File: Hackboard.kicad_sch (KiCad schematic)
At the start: 70 parts, among them J1 Conn_01x23_Socket, J2 Micro_SD_Card, J3 Conn_01x32_Socket, J4 Conn_01x08_Socket, J5 Conn_01x02_Pin, J6 USB_C_Receptacle_USB2.0_16P, J7 Barrel_Jack_Switch, Q1 NMOS, Q2 NMOS, Q3 NMOS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

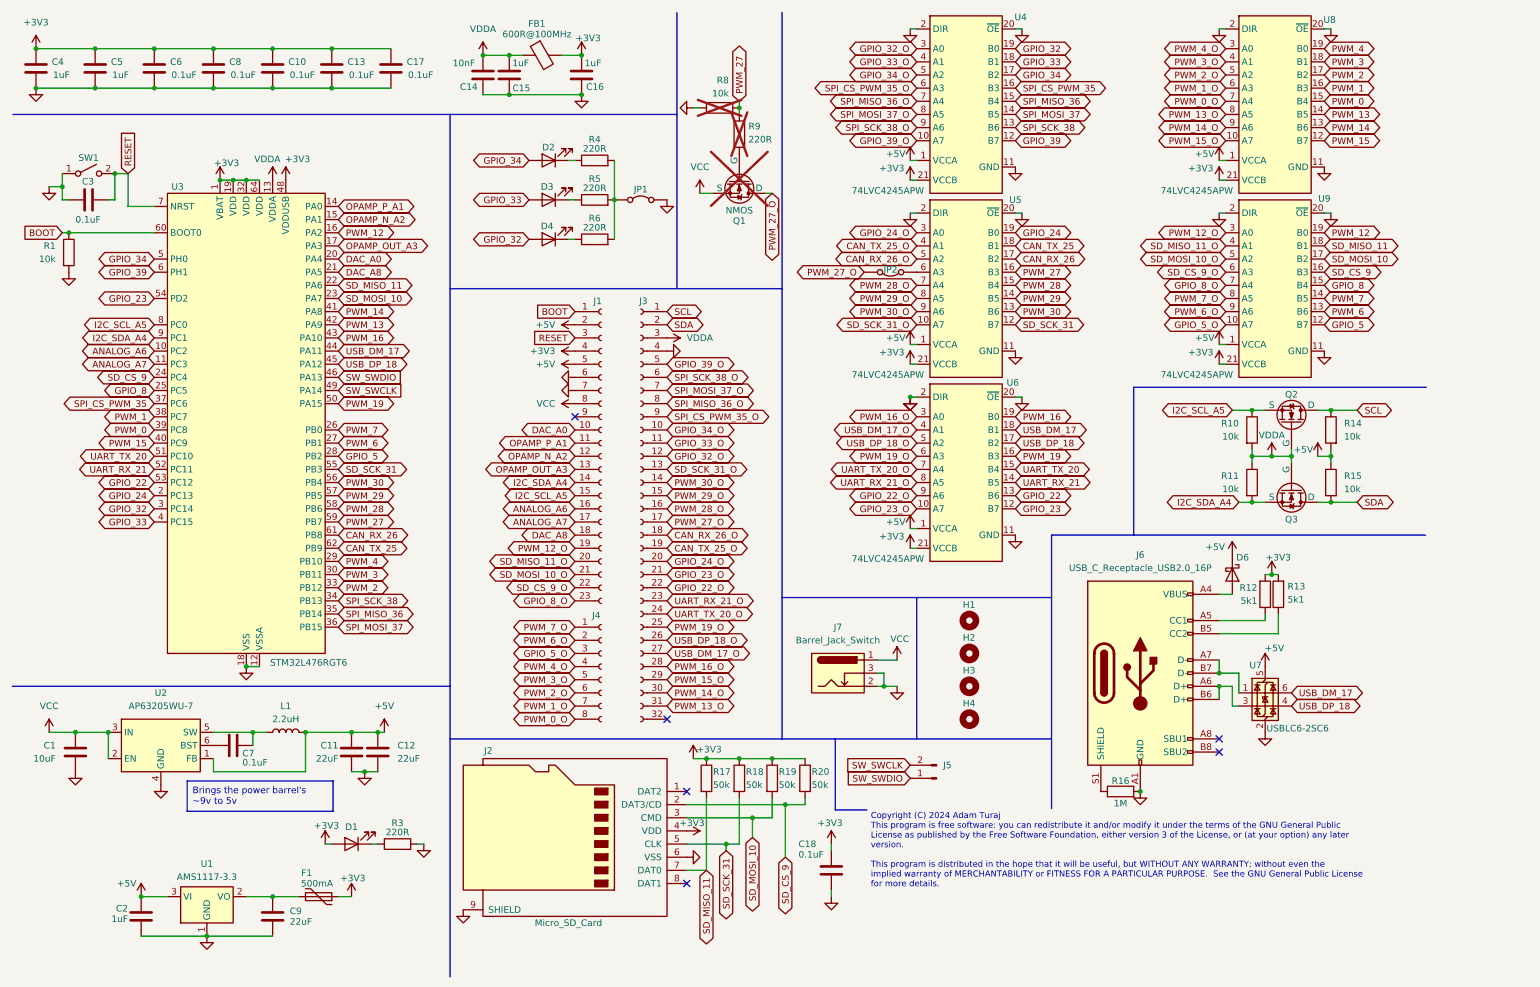
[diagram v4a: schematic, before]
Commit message: Add reverse polarity protection, remove logic shifters, make misc changes to schematic
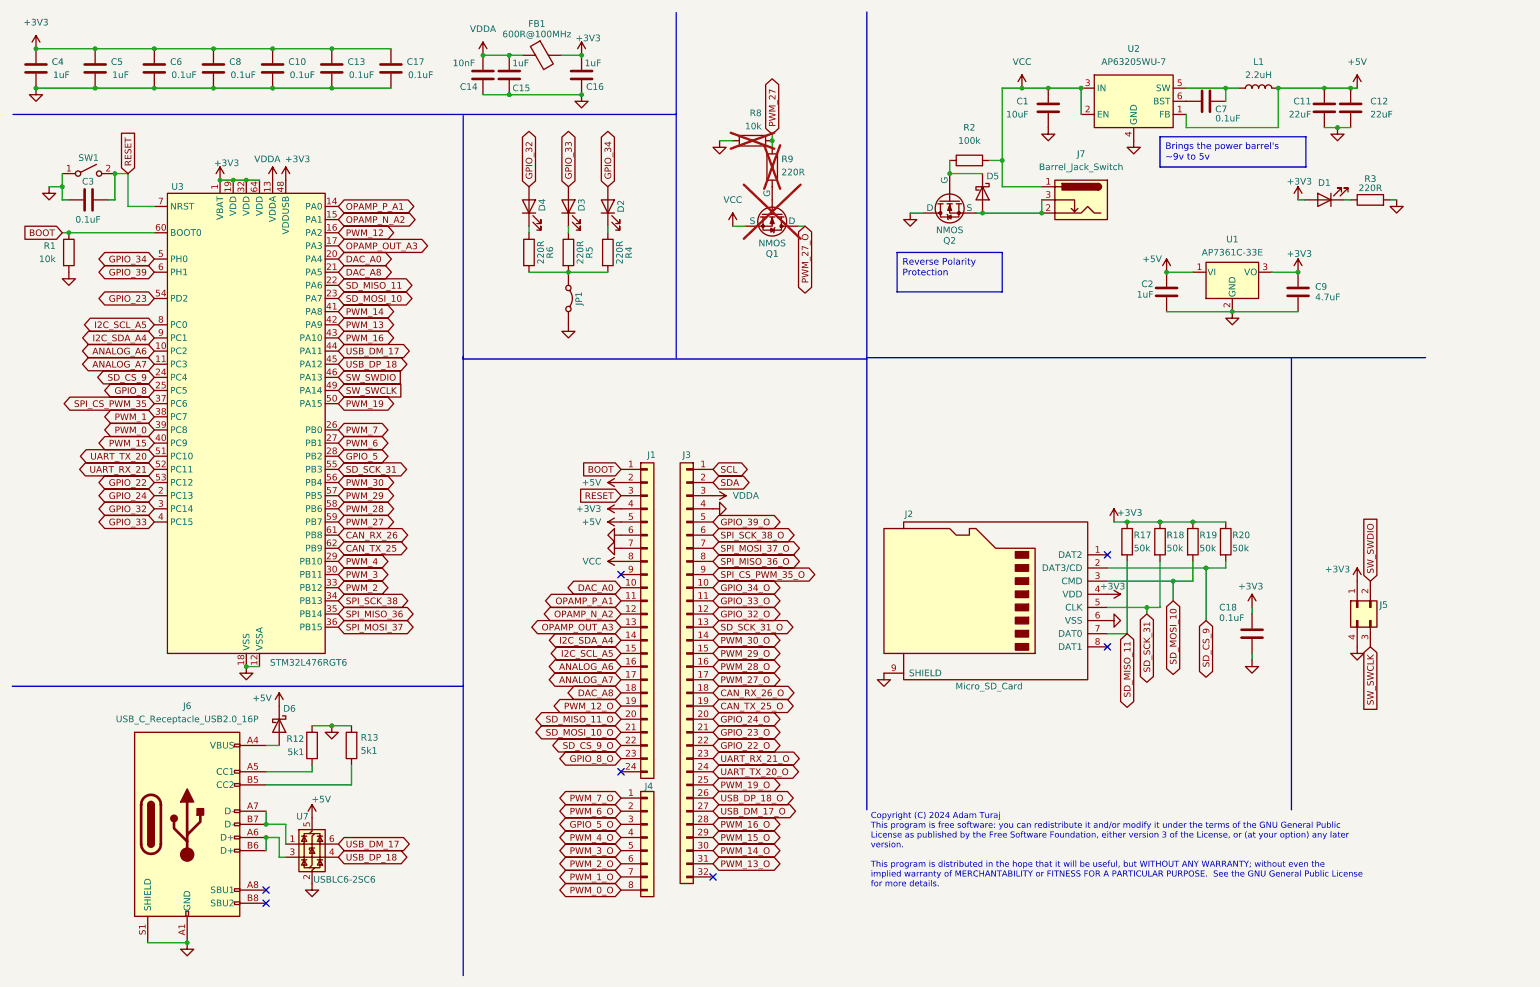
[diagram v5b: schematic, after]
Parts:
- removed F1: 500mA, Fuse:Fuse_1812_4532Metric, symbol Device:Polyfuse
- removed H1, H2, H3, H4: MountingHole, MountingHole:MountingHole_3.2mm_M3, symbol Mechanical:MountingHole
- removed J1: Conn_01x23_Socket, Connector_PinHeader_2.54mm:PinHeader_1x23_P2.54mm_Vertical, symbol Connector:Conn_01x23_Socket
- removed J3: Conn_01x32_Socket, Connector_PinHeader_2.54mm:PinHeader_1x32_P2.54mm_Vertical, symbol Connector:Conn_01x32_Socket
- removed J4: Conn_01x08_Socket, Connector_PinHeader_2.54mm:PinHeader_1x08_P2.54mm_Vertical, symbol Connector:Conn_01x08_Socket
- removed J5: Conn_01x02_Pin, Connector_PinHeader_2.54mm:PinHeader_1x02_P2.54mm_Vertical, symbol Connector:Conn_01x02_Pin
- removed JP2: Jumper_2_Bridged, Jumper:SolderJumper-2_P1.3mm_Open_RoundedPad1.0x1.5mm, symbol Jumper:Jumper_2_Bridged
- removed Q3: NMOS, Package_TO_SOT_SMD:SOT-23, symbol Simulation_SPICE:NMOS
- removed R10, R11, R14, R15: 10k, Resistor_SMD:R_0603_1608Metric, symbol Device:R
- removed R16: 1M, Resistor_SMD:R_0603_1608Metric, symbol Device:R
- removed U1: AMS1117-3.3, Package_TO_SOT_SMD:SOT-223-3_TabPin2, symbol Regulator_Linear:AMS1117-3.3
- removed U4, U5, U6, U8, U9: 74LVC4245APW, Package_SO:TSSOP-24_4.4x7.8mm_P0.65mm, symbol 74LVC4245A:74LVC4245A
- added D5: D_Schottky, DO-221AC:VSSAF3L63HM3, symbol Device:D_Schottky
- added J1: Conn_01x24, symbol Connector_Generic:Conn_01x24
- added J3: Conn_01x32, symbol Connector_Generic:Conn_01x32
- added J4: Conn_01x08, symbol Connector_Generic:Conn_01x08
- added J5: Conn_02x02_Counter_Clockwise, symbol Connector_Generic:Conn_02x02_Counter_Clockwise
- added R2: 100k, symbol Device:R
- added U1: AP7361C-33E, Package_TO_SOT_SMD:SOT-223-3_TabPin2, symbol Regulator_Linear:AP7361C-33E
- C9: value 22uF -> 4.7uF; MPN CC0603KRX7R7BB105 -> AP7361-33E-13
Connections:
- net +3V3: now also C9.2, J1.4 (Pin_4), J5.1 (Pin_1), U1.3 (VO); no longer R12.2, R13.2
- net +5V: now also J1.2 (Pin_2), J1.5 (Pin_5), U1.1 (VI)
- net ANALOG_A6: now also J1.16 (Pin_16)
- net ANALOG_A7: now also J1.17 (Pin_17)
- net BOOT: now also J1.1 (Pin_1)
- net CAN_RX_26_O: now also J3.18 (Pin_18)
- net CAN_TX_25_O: now also J3.19 (Pin_19)
- net DAC_A0: now also J1.10 (Pin_10)
- net DAC_A8: now also J1.18 (Pin_18)
- net GND: now also J6.S1 (SHIELD), Q2.1 (D), R12.2, R13.2, J1.6 (Pin_6), J1.7 (Pin_7), J3.4 (Pin_4), J5.4 (Pin_4), U1.2 (GND); no longer J7.2, J7.3
- net GPIO_22_O: now also J3.22 (Pin_22)
- net GPIO_23_O: now also J3.21 (Pin_21)
- net GPIO_24_O: now also J3.20 (Pin_20)
- net GPIO_32_O: now also J3.12 (Pin_12)
- net GPIO_33_O: now also J3.11 (Pin_11)
- net GPIO_34_O: now also J3.10 (Pin_10)
- net GPIO_39_O: now also J3.5 (Pin_5)
- net GPIO_5_O: now also J4.3 (Pin_3)
- net GPIO_8_O: now also J1.23 (Pin_23)
- net I2C_SCL_A5: now also J1.15 (Pin_15); no longer Q2.3 (S)
- net I2C_SDA_A4: now also J1.14 (Pin_14)
- net OPAMP_N_A2: now also J1.12 (Pin_12)
- net OPAMP_OUT_A3: now also J1.13 (Pin_13)
- net OPAMP_P_A1: now also J1.11 (Pin_11)
- net PWM_0_O: now also J4.8 (Pin_8)
- net PWM_12_O: now also J1.19 (Pin_19)
- net PWM_13_O: now also J3.31 (Pin_31)
- net PWM_14_O: now also J3.30 (Pin_30)
- net PWM_15_O: now also J3.29 (Pin_29)
- net PWM_16_O: now also J3.28 (Pin_28)
- net PWM_19_O: now also J3.25 (Pin_25)
- net PWM_1_O: now also J4.7 (Pin_7)
- net PWM_27_O: now also J3.17 (Pin_17)
- net PWM_28_O: now also J3.16 (Pin_16)
- net PWM_29_O: now also J3.15 (Pin_15)
- net PWM_2_O: now also J4.6 (Pin_6)
- net PWM_30_O: now also J3.14 (Pin_14)
- net PWM_3_O: now also J4.5 (Pin_5)
- net PWM_4_O: now also J4.4 (Pin_4)
- net PWM_6_O: now also J4.2 (Pin_2)
- net PWM_7_O: now also J4.1 (Pin_1)
- net RESET: now also J1.3 (Pin_3)
- net SCL: now also J3.1 (Pin_1); no longer Q2.1 (D)
- net SDA: now also J3.2 (Pin_2)
- net SD_CS_9_O: now also J1.22 (Pin_22)
- net SD_MISO_11_O: now also J1.20 (Pin_20)
- net SD_MOSI_10_O: now also J1.21 (Pin_21)
- net SD_SCK_31_O: now also J3.13 (Pin_13)
- net SPI_CS_PWM_35_O: now also J3.9 (Pin_9)
- net SPI_MISO_36_O: now also J3.8 (Pin_8)
- net SPI_MOSI_37_O: now also J3.7 (Pin_7)
- net SPI_SCK_38_O: now also J3.6 (Pin_6)
- net SW_SWCLK: now also J5.3 (Pin_3)
- net SW_SWDIO: now also J5.2 (Pin_2)
- net UART_RX_21_O: now also J3.23 (Pin_23)
- net UART_TX_20_O: now also J3.24 (Pin_24)
- net USB_DM_17_O: now also J3.27 (Pin_27)
- net USB_DP_18_O: now also J3.26 (Pin_26)
- net VCC: now also J1.8 (Pin_8), R2.2
- net VDDA: now also J3.3 (Pin_3); no longer Q2.2 (G)
- new net: D5.2 (A), J7.2, J7.3, Q2.3 (S)
- new net: D5.1 (K), Q2.2 (G), R2.1
- no-connect marks 6 -> 7
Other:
- moved on the sheet: C1, C11, C12, C18, C2, C7, C9, D1, D2, D3, D4, D6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

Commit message: Finish making changes to schematic
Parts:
- removed J3: Conn_01x32, symbol Connector_Generic:Conn_01x32
- removed J4: Conn_01x08, symbol Connector_Generic:Conn_01x08
- added C19, C20: 10pF, Capacitor_SMD:C_0603_1608Metric, symbol Device:C
- added J3, J4: Conn_01x09, Headers:PinSocket_1x09_P2.54mm_Vertical, symbol Connector_Generic:Conn_01x09
- added J8: Conn_01x22, Headers:PinSocket_1x22_P2.54mm_Vertical, symbol Connector_Generic:Conn_01x22
- added Y1: 48MHz, Oscillator:Oscillator_SMD_Abracon_ASE-4Pin_3.2x2.5mm_HandSoldering, symbol Device:Crystal_GND23
- D4: LCSC C2286 -> (none)
- D5, D6, FB1: LCSC C780074 -> (none)
- J1: footprint (none) -> Headers:PinSocket_1x24_P2.54mm_Vertical
- J5: footprint (none) -> Connector_PinHeader_2.54mm:PinHeader_2x02_P2.54mm_Vertical
- Q1, Q2: LCSC C15127 -> (none)
- R2: footprint (none) -> Resistor_SMD:R_0603_1608Metric
- R3, R4, R5, R6: value 220R -> 240R
- U1: MPN (none) -> AP7361C-33E-13
- U2: LCSC C2071056 -> (none)
- U3: LCSC C74797 -> (none)
- U7: LCSC C7519 -> (none)
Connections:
- net GPIO_8_O is gone; now on net SD_CS_9: J1.23 (Pin_23)
- net SD_CS_9_O is gone; now on net SD_MOSI_10: J1.22 (Pin_22)
- net SD_MISO_11_O is gone; now on net PWM_12: J1.20 (Pin_20)
- net SD_MOSI_10_O is gone; now on net SD_MISO_11: J1.21 (Pin_21)
- net CAN_RX_26: now also J8.7 (Pin_7)
- net CAN_TX_25: now also J8.9 (Pin_9)
- net GND: now also C19.2, C20.2, J3.4 (Pin_4), Y1.2, Y1.3
- net GPIO_22: now also J8.12 (Pin_12)
- net GPIO_23: now also J8.11 (Pin_11)
- net GPIO_24: now also J8.10 (Pin_10)
- net GPIO_32: now also J8.1 (Pin_1)
- net GPIO_33: now also J3.9 (Pin_9)
- net GPIO_34: no longer U3.5 (PH0)
- net GPIO_5: now also J4.3 (Pin_3)
- net GPIO_8: now also J1.24 (Pin_24)
- net PWM_0: now also J4.9 (Pin_9)
- net PWM_1: now also J4.8 (Pin_8)
- net PWM_13: now also J8.22 (Pin_22)
- net PWM_14: now also J8.21 (Pin_21)
- net PWM_15: now also J8.20 (Pin_20)
- net PWM_16: now also J8.19 (Pin_19)
- net PWM_19: now also J8.15 (Pin_15)
- net PWM_2: now also J4.7 (Pin_7)
- net PWM_27: now also J8.6 (Pin_6)
- net PWM_28: now also J8.5 (Pin_5)
- net PWM_29: now also J8.4 (Pin_4)
- net PWM_3: now also J4.6 (Pin_6)
- net PWM_30: now also J8.3 (Pin_3)
- net PWM_4: now also J4.4 (Pin_4)
- net PWM_6: now also J4.2 (Pin_2)
- net PWM_7: now also J4.1 (Pin_1)
- net SCL: now also J3.1 (Pin_1)
- net SDA: now also J3.2 (Pin_2)
- net SD_SCK_31: now also J8.2 (Pin_2)
- net UART_RX_21: now also J8.13 (Pin_13)
- net UART_TX_20: now also J8.14 (Pin_14)
- net USB_DM_17: now also J8.18 (Pin_18)
- net USB_DP_18: now also J8.17 (Pin_17)
- net VDDA: now also J3.3 (Pin_3)
- net GPIO_39: no longer names the net of U3.6 (PH1)
- net GPIO_39: now also C19.1, Y1.1
- net PWM_12_O: no longer names the net of J1.19 (Pin_19)
- new net: C20.1, U3.5 (PH0), Y1.4
- new net SPI_CS_PWM_34: J3.8 (Pin_8)
- new net SPI_MISO_35: J3.7 (Pin_7)
- new net SPI_MOSI_36: J3.6 (Pin_6)
- new net SPI_SCK_37: J3.5 (Pin_5)
- no-connect marks 7 -> 9
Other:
- moved on the sheet: C2, C3, C9, R1, SW1, U1
